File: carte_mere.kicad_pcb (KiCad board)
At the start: 4 copper layers, 78 parts, among them J1 Conn_01x02_Pin, J10 Conn_01x03_Pin, J11 Conn_01x03_Pin, J12 Conn_01x03_Pin, J13 Conn_01x03_Pin, J14 Conn_01x03_Pin, J15 Conn_01x03_Pin, J2 Conn_01x03_Pin, J25 Conn_01x02_Pin, J26 Conn_01x02_Pin, J27 Conn_01x02_Pin, J28 Conn_01x02_Pin, J29 Conn_01x02_Pin, J3 Conn_01x03_Pin, J30 Conn_01x02_Pin, J4 Conn_01x03_Pin, J5 Conn_01x03_Pin, J6 Conn_01x03_Pin, J7 Conn_01x03_Pin, J8 Conn_01x03_Pin, J9 Conn_01x03_Pin, Q1 MMBT3906, Q10 2N7002, Q11 MMBT3906, Q12 AO3401A, Q13 2N7002, Q14 MMBT3906, Q15 AO3401A, Q16 2N7002, Q17 MMBT3906, Q18 AO3401A, Q2 2N7002, Q3 AO3401A, Q4 2N7002, Q5 MMBT3906, Q6 AO3401A, Q7 2N7002, Q8 MMBT3906, Q9 AO3401A, U1 SN65HVD230, U2 SN74LVC1T45DBV, U3 R-78B3.3-2.0, U4 R-78B5.0-2.0

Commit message: update
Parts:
- removed C1, C2: 22uF, Capacitor_SMD:CP_Elec_5x5.4
- removed D3, D4: D_Small, Diode_SMD:D_SMA_Handsoldering
- removed J11, J12, J13, J14, J15: Conn_01x03_Pin, Connector_JST:JST_XH_B3B-XH-AM_1x03_P2.50mm_Vertical
- removed U3: R-78B3.3-2.0, Converter_DCDC:Converter_DCDC_RECOM_R-78B-2.0_THT
- removed U4: R-78B5.0-2.0, Converter_DCDC:Converter_DCDC_RECOM_R-78B-2.0_THT
- added C10: 47µF 6.3V, Capacitor_SMD:C_0805_2012Metric, F.Cu at (178.2, 113.8)
- added C11: 47µF 6.3V, Capacitor_SMD:C_0805_2012Metric, F.Cu at (178.2, 117.9)
- added C12: 47µF 6.3V, Capacitor_SMD:C_0805_2012Metric, F.Cu at (178.2, 120.0)
- added C13: 22µF 25V, Capacitor_SMD:C_0805_2012Metric, F.Cu at (191.0, 122.6)
- added C14: 22µF 25V, Capacitor_SMD:C_0805_2012Metric, F.Cu at (202.4, 119.5)
- added C15: 220nF 16V, Capacitor_SMD:C_0402_1005Metric, F.Cu at (202.6, 112.5)
- added C16: 150pF 50V, Capacitor_SMD:C_0603_1608Metric, F.Cu at (207.1, 116.7)
- added C17: 22µF 25V, Capacitor_SMD:C_0805_2012Metric, F.Cu at (192.1, 113.0)
- added C18: 22µF 25V, Capacitor_SMD:C_0805_2012Metric, F.Cu at (192.1, 115.2)
- added C19: 22µF 25V, Capacitor_SMD:C_0805_2012Metric, F.Cu at (192.1, 119.4)
- added C20: 22µF 25V, Capacitor_SMD:C_0805_2012Metric, F.Cu at (192.1, 117.3)
- added C21: 22µF 25V, Capacitor_SMD:C_0805_2012Metric, F.Cu at (200.9, 122.5)
- added C22: 22µF 25V, Capacitor_SMD:C_0805_2012Metric, F.Cu at (204.7, 119.5)
- added C3: 22µF 25V, Capacitor_SMD:C_0805_2012Metric, F.Cu at (180.1, 122.4)
- added C4: 22µF 25V, Capacitor_SMD:C_0805_2012Metric, F.Cu at (165.8, 114.5)
- added C5: 22µF 25V, Capacitor_SMD:C_0805_2012Metric, F.Cu at (168.0, 114.5)
- added C6: 220nF 16V, Capacitor_SMD:C_0402_1005Metric, F.Cu at (168.1, 120.5)
- added C7: 150pF 50V, Capacitor_SMD:C_0603_1608Metric, F.Cu at (163.4, 116.1)
- added C8: 47µF 6.3V, Capacitor_SMD:C_0805_2012Metric, F.Cu at (169.1, 111.5)
- added C9: 47µF 6.3V, Capacitor_SMD:C_0805_2012Metric, F.Cu at (178.2, 115.8)
- added D1: LED, LED_SMD:LED_0201_0603Metric_Pad0.64x0.40mm_HandSolder, F.Cu at (165.7, 106.3)
- added D2: LED, LED_SMD:LED_0201_0603Metric_Pad0.64x0.40mm_HandSolder, F.Cu at (180.6, 87.6)
- added J16: Conn_01x03_Pin, 7Robot_Conn:Molex_SPOX_5267-03A_1x03_P2.50mm_Vertical, F.Cu at (185.6, 83.0)
- added J17: Conn_01x05_Pin, Connector_PinHeader_2.54mm:PinHeader_1x05_P2.54mm_Vertical, F.Cu at (126.1, 104.5)
- added J18: Conn_01x05_Pin, Connector_PinHeader_2.54mm:PinHeader_1x05_P2.54mm_Vertical, F.Cu at (130.8, 104.5)
- added J19: Conn_01x05_Pin, Connector_PinHeader_2.54mm:PinHeader_1x05_P2.54mm_Vertical, F.Cu at (135.4, 104.5)
- added J31: Conn_01x03_Pin, Connector_JST:JST_XH_B3B-XH-AM_1x03_P2.50mm_Vertical, F.Cu at (92.2, 56.8)
- added J32: Conn_01x03_Pin, Connector_JST:JST_XH_B3B-XH-AM_1x03_P2.50mm_Vertical, F.Cu at (92.2, 64.6)
- added J33: Conn_01x03_Pin, Connector_JST:JST_XH_B3B-XH-AM_1x03_P2.50mm_Vertical, F.Cu at (92.2, 72.4)
- added J34: Conn_01x03_Pin, Connector_JST:JST_XH_B3B-XH-AM_1x03_P2.50mm_Vertical, F.Cu at (92.2, 80.2)
- added J35: Conn_01x03_Pin, Connector_JST:JST_XH_B3B-XH-AM_1x03_P2.50mm_Vertical, F.Cu at (104.2, 56.8)
- added J36: Conn_01x03_Pin, Connector_JST:JST_XH_B3B-XH-AM_1x03_P2.50mm_Vertical, F.Cu at (104.2, 64.6)
- added J37: Conn_01x03_Pin, Connector_JST:JST_XH_B3B-XH-AM_1x03_P2.50mm_Vertical, F.Cu at (104.2, 72.4)
- added J38: Conn_01x03_Pin, Connector_JST:JST_XH_B3B-XH-AM_1x03_P2.50mm_Vertical, F.Cu at (104.2, 80.2)
- added JP1: ~, Z7-lite:Z7-lite, F.Cu at (157.8, 55.9)
- added L1: PSPMAQ0605H-150M-ANP, 7Robot_lib:Prod_Tech_7.1x6.6mm, F.Cu at (172.8, 117.2)
- added L2: PSPMAQ0605H-150M-ANP, 7Robot_lib:Prod_Tech_7.1x6.6mm, F.Cu at (197.6, 115.8)
- added Q19: 2N7002, Package_TO_SOT_SMD:SOT-23, F.Cu at (67.3, 87.0)
- added Q20: 2N7002, Package_TO_SOT_SMD:SOT-23, F.Cu at (67.3, 91.6)
- added Q21: 2N7002, Package_TO_SOT_SMD:SOT-23, F.Cu at (67.3, 96.2)
- added Q22: 2N7002, Package_TO_SOT_SMD:SOT-23, F.Cu at (67.3, 100.9)
- added Q23: 2N7002, Package_TO_SOT_SMD:SOT-23, F.Cu at (72.2, 87.0)
- added Q24: 2N7002, Package_TO_SOT_SMD:SOT-23, F.Cu at (72.2, 91.6)
- added Q25: 2N7002, Package_TO_SOT_SMD:SOT-23, F.Cu at (72.2, 96.2)
- added Q26: 2N7002, Package_TO_SOT_SMD:SOT-23, F.Cu at (72.2, 100.9)
- added Q27: 2N7002, Package_TO_SOT_SMD:SOT-23, F.Cu at (77.1, 87.0)
- added Q28: 2N7002, Package_TO_SOT_SMD:SOT-23, F.Cu at (77.1, 91.6)
- added Q29: 2N7002, Package_TO_SOT_SMD:SOT-23, F.Cu at (77.1, 96.2)
- added Q30: 2N7002, Package_TO_SOT_SMD:SOT-23, F.Cu at (77.1, 100.9)
- added Q31: 2N7002, Package_TO_SOT_SMD:SOT-23, F.Cu at (82.0, 87.0)
- added Q32: 2N7002, Package_TO_SOT_SMD:SOT-23, F.Cu at (82.0, 91.6)
- added Q33: 2N7002, Package_TO_SOT_SMD:SOT-23, F.Cu at (82.0, 96.2)
- added Q34: 2N7002, Package_TO_SOT_SMD:SOT-23, F.Cu at (82.0, 100.9)
- added R1: 100R, Resistor_SMD:R_0201_0603Metric_Pad0.64x0.40mm_HandSolder, F.Cu at (162.2, 101.6)
- added R10: 1k, Resistor_SMD:R_0201_0603Metric_Pad0.64x0.40mm_HandSolder, F.Cu at (139.1, 106.6)
- added R100: 10k, Resistor_SMD:R_0201_0603Metric_Pad0.64x0.40mm_HandSolder, F.Cu at (99.8, 96.0)
- added R101: 10k, Resistor_SMD:R_0201_0603Metric_Pad0.64x0.40mm_HandSolder, F.Cu at (99.8, 97.7)
- added R103: 9.1k, Resistor_SMD:R_0603_1608Metric, F.Cu at (207.1, 113.5)
- added R104: 68k, Resistor_SMD:R_0603_1608Metric, F.Cu at (207.9, 120.0)
- added R11: 10k, Resistor_SMD:R_0201_0603Metric_Pad0.64x0.40mm_HandSolder, F.Cu at (85.8, 90.7)
- added R12: 2k, Resistor_SMD:R_0201_0603Metric_Pad0.64x0.40mm_HandSolder, F.Cu at (139.1, 108.3)
- added R13: 100R, Resistor_SMD:R_0201_0603Metric_Pad0.64x0.40mm_HandSolder, F.Cu at (85.8, 92.5)
- added R14: 1k, Resistor_SMD:R_0201_0603Metric_Pad0.64x0.40mm_HandSolder, F.Cu at (139.1, 110.1)
- added R15: 10k, Resistor_SMD:R_0201_0603Metric_Pad0.64x0.40mm_HandSolder, F.Cu at (85.8, 94.2)
- added R16: 2k, Resistor_SMD:R_0201_0603Metric_Pad0.64x0.40mm_HandSolder, F.Cu at (139.1, 111.8)
- added R17: 100R, Resistor_SMD:R_0201_0603Metric_Pad0.64x0.40mm_HandSolder, F.Cu at (85.8, 96.0)
- added R18: 10k, Resistor_SMD:R_0201_0603Metric_Pad0.64x0.40mm_HandSolder, F.Cu at (85.8, 97.7)
- added R19: 100R, Resistor_SMD:R_0201_0603Metric_Pad0.64x0.40mm_HandSolder, F.Cu at (88.6, 85.5)
- added R2: 100R, Resistor_SMD:R_0201_0603Metric_Pad0.64x0.40mm_HandSolder, F.Cu at (162.1, 104.5)
- added R20: 1k, Resistor_SMD:R_0201_0603Metric_Pad0.64x0.40mm_HandSolder, F.Cu at (139.1, 113.6)
- added R21: 2k, Resistor_SMD:R_0201_0603Metric_Pad0.64x0.40mm_HandSolder, F.Cu at (141.9, 103.1)
- added R22: 1k, Resistor_SMD:R_0201_0603Metric_Pad0.64x0.40mm_HandSolder, F.Cu at (141.9, 104.8)
- added R23: 10k, Resistor_SMD:R_0201_0603Metric_Pad0.64x0.40mm_HandSolder, F.Cu at (88.6, 87.2)
- added R24: 10k, Resistor_SMD:R_0201_0603Metric_Pad0.64x0.40mm_HandSolder, F.Cu at (88.6, 89.0)
- added R25: 10k, Resistor_SMD:R_0201_0603Metric_Pad0.64x0.40mm_HandSolder, F.Cu at (88.6, 90.7)
- added R26: 2k, Resistor_SMD:R_0201_0603Metric_Pad0.64x0.40mm_HandSolder, F.Cu at (141.9, 106.6)
- added R27: 1k, Resistor_SMD:R_0201_0603Metric_Pad0.64x0.40mm_HandSolder, F.Cu at (141.9, 108.3)
- added R28: 2k, Resistor_SMD:R_0201_0603Metric_Pad0.64x0.40mm_HandSolder, F.Cu at (141.9, 110.1)
- added R29: 18k, Resistor_SMD:R_0603_1608Metric, F.Cu at (163.5, 119.1)
- added R3: 1k, Resistor_SMD:R_0201_0603Metric_Pad0.64x0.40mm_HandSolder, F.Cu at (163.8, 106.3)
- added R30: 1k, Resistor_SMD:R_0201_0603Metric_Pad0.64x0.40mm_HandSolder, F.Cu at (141.9, 111.8)
- added R31: 82k, Resistor_SMD:R_0603_1608Metric, F.Cu at (163.0, 113.6)
- added R32: 2k, Resistor_SMD:R_0201_0603Metric_Pad0.64x0.40mm_HandSolder, F.Cu at (141.9, 113.6)
- added R33: 1k, Resistor_SMD:R_0201_0603Metric_Pad0.64x0.40mm_HandSolder, F.Cu at (178.4, 87.6)
- added R34: 100k, Resistor_SMD:R_0201_0603Metric_Pad0.64x0.40mm_HandSolder, F.Cu at (177.8, 83.2)
- added R35: 100R, Resistor_SMD:R_0201_0603Metric_Pad0.64x0.40mm_HandSolder, F.Cu at (176.3, 86.8)
- added R36: 100R, Resistor_SMD:R_0201_0603Metric_Pad0.64x0.40mm_HandSolder, F.Cu at (181.5, 85.9)
- added R37: 10k, Resistor_SMD:R_0201_0603Metric_Pad0.64x0.40mm_HandSolder, F.Cu at (180.5, 83.2)
- added R4: 1k, Resistor_SMD:R_0201_0603Metric_Pad0.64x0.40mm_HandSolder, F.Cu at (170.7, 103.0)
- added R5: 1k, Resistor_SMD:R_0201_0603Metric_Pad0.64x0.40mm_HandSolder, F.Cu at (139.1, 103.1)
- added R6: 10k, Resistor_SMD:R_0201_0603Metric_Pad0.64x0.40mm_HandSolder, F.Cu at (85.8, 85.5)
- added R64: 20k, Resistor_SMD:R_0201_0603Metric, F.Cu at (125.3, 99.3)
- added R66: 100R, Resistor_SMD:R_0201_0603Metric_Pad0.64x0.40mm_HandSolder, F.Cu at (88.6, 92.5)
- added R67: 10k, Resistor_SMD:R_0201_0603Metric_Pad0.64x0.40mm_HandSolder, F.Cu at (88.6, 94.2)
- added R68: 10k, Resistor_SMD:R_0201_0603Metric_Pad0.64x0.40mm_HandSolder, F.Cu at (88.6, 96.0)
- added R69: 100R, Resistor_SMD:R_0201_0603Metric_Pad0.64x0.40mm_HandSolder, F.Cu at (88.6, 97.7)
- added R7: 100R, Resistor_SMD:R_0201_0603Metric_Pad0.64x0.40mm_HandSolder, F.Cu at (85.8, 87.2)
- added R70: 10k, Resistor_SMD:R_0201_0603Metric_Pad0.64x0.40mm_HandSolder, F.Cu at (91.4, 85.5)
- added R71: 10k, Resistor_SMD:R_0201_0603Metric_Pad0.64x0.40mm_HandSolder, F.Cu at (91.4, 87.2)
- added R72: 100R, Resistor_SMD:R_0201_0603Metric_Pad0.64x0.40mm_HandSolder, F.Cu at (91.4, 89.0)
- added R73: 10k, Resistor_SMD:R_0201_0603Metric_Pad0.64x0.40mm_HandSolder, F.Cu at (91.4, 90.7)
- added R74: 10k, Resistor_SMD:R_0201_0603Metric_Pad0.64x0.40mm_HandSolder, F.Cu at (91.4, 92.5)
- added R75: 100R, Resistor_SMD:R_0201_0603Metric_Pad0.64x0.40mm_HandSolder, F.Cu at (91.4, 94.2)
- added R76: 10k, Resistor_SMD:R_0201_0603Metric_Pad0.64x0.40mm_HandSolder, F.Cu at (91.4, 96.0)
- added R77: 10k, Resistor_SMD:R_0201_0603Metric_Pad0.64x0.40mm_HandSolder, F.Cu at (91.4, 97.7)
- added R78: 100R, Resistor_SMD:R_0201_0603Metric_Pad0.64x0.40mm_HandSolder, F.Cu at (94.2, 85.5)
- added R79: 10k, Resistor_SMD:R_0201_0603Metric_Pad0.64x0.40mm_HandSolder, F.Cu at (94.2, 87.2)
- added R8: 2k, Resistor_SMD:R_0201_0603Metric_Pad0.64x0.40mm_HandSolder, F.Cu at (139.1, 104.8)
- added R80: 10k, Resistor_SMD:R_0201_0603Metric_Pad0.64x0.40mm_HandSolder, F.Cu at (94.2, 89.0)
- added R81: 100R, Resistor_SMD:R_0201_0603Metric_Pad0.64x0.40mm_HandSolder, F.Cu at (94.2, 90.7)
- added R82: 10k, Resistor_SMD:R_0201_0603Metric_Pad0.64x0.40mm_HandSolder, F.Cu at (94.2, 92.5)
- added R83: 10k, Resistor_SMD:R_0201_0603Metric_Pad0.64x0.40mm_HandSolder, F.Cu at (94.2, 94.2)
- added R84: 100R, Resistor_SMD:R_0201_0603Metric_Pad0.64x0.40mm_HandSolder, F.Cu at (94.2, 96.0)
- added R85: 10k, Resistor_SMD:R_0201_0603Metric_Pad0.64x0.40mm_HandSolder, F.Cu at (94.2, 97.7)
- added R86: 10k, Resistor_SMD:R_0201_0603Metric_Pad0.64x0.40mm_HandSolder, F.Cu at (97.0, 85.5)
- added R87: 100R, Resistor_SMD:R_0201_0603Metric_Pad0.64x0.40mm_HandSolder, F.Cu at (97.0, 87.2)
- added R88: 10k, Resistor_SMD:R_0201_0603Metric_Pad0.64x0.40mm_HandSolder, F.Cu at (97.0, 89.0)
- added R89: 10k, Resistor_SMD:R_0201_0603Metric_Pad0.64x0.40mm_HandSolder, F.Cu at (97.0, 90.7)
- added R9: 10k, Resistor_SMD:R_0201_0603Metric_Pad0.64x0.40mm_HandSolder, F.Cu at (85.8, 89.0)
- added R90: 100R, Resistor_SMD:R_0201_0603Metric_Pad0.64x0.40mm_HandSolder, F.Cu at (97.0, 92.5)
- added R91: 10k, Resistor_SMD:R_0201_0603Metric_Pad0.64x0.40mm_HandSolder, F.Cu at (97.0, 94.2)
- added R92: 10k, Resistor_SMD:R_0201_0603Metric_Pad0.64x0.40mm_HandSolder, F.Cu at (97.0, 96.0)
- added R93: 100R, Resistor_SMD:R_0201_0603Metric_Pad0.64x0.40mm_HandSolder, F.Cu at (97.0, 97.7)
- added R94: 10k, Resistor_SMD:R_0201_0603Metric_Pad0.64x0.40mm_HandSolder, F.Cu at (99.8, 85.5)
- added R95: 10k, Resistor_SMD:R_0201_0603Metric_Pad0.64x0.40mm_HandSolder, F.Cu at (99.8, 87.2)
- added R96: 100R, Resistor_SMD:R_0201_0603Metric_Pad0.64x0.40mm_HandSolder, F.Cu at (99.8, 89.0)
- added R97: 10k, Resistor_SMD:R_0201_0603Metric_Pad0.64x0.40mm_HandSolder, F.Cu at (99.8, 90.7)
- added R98: 10k, Resistor_SMD:R_0201_0603Metric_Pad0.64x0.40mm_HandSolder, F.Cu at (99.8, 92.5)
- added R99: 100R, Resistor_SMD:R_0201_0603Metric_Pad0.64x0.40mm_HandSolder, F.Cu at (99.8, 94.2)
- added U5: TPS54302, Package_TO_SOT_SMD:SOT-23-6, F.Cu at (166.9, 118.1)
- added U6: TPS54302, Package_TO_SOT_SMD:SOT-23-6, F.Cu at (203.5, 114.9)
- J10: value Conn_01x03_Pin -> Conn_01x02_Pin; footprint Connector_JST:JST_XH_B3B-XH-AM_1x03_P2.50mm_Vertical -> Connector_AMASS:AMASS_XT30U-F_1x02_P5.0mm_Vertical
- moved J1 270.8 mm to (173.9, 104.3), turned to 90 degrees
- moved H3 265.7 mm to (209.3, 125.0)
- moved U1 261.3 mm to (166.4, 103.0)
- moved U2 258.3 mm to (178.9, 85.4)
- moved J10 237.9 mm to (185.9, 115.0), turned to -90 degrees
- moved R38 233.2 mm to (144.8, 103.1)
- moved R39 233.2 mm to (144.8, 104.8)
- moved R40 233.2 mm to (144.8, 106.6)
- moved R41 233.2 mm to (144.8, 108.3)
- moved J25 216.3 mm to (118.1, 56.8)
- moved J27 216.3 mm to (118.1, 72.4)
- moved J28 216.3 mm to (118.1, 80.2)
- moved J29 216.3 mm to (118.1, 88.0)
- moved J30 216.3 mm to (118.1, 95.8)
- moved Q13 216.3 mm to (136.3, 62.5)
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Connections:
- net +5V renamed 5V
- J10 pad 2: 5V_POWER -> 24V
- U1 pad 3: +3V3 -> 3.3V
- U2 pad 1: +3.3V -> 3.3V
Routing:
- net GND: track 0.00 -> 25.1 mm, vias 0 -> 56
- net 3.3V: track 0.00 -> 19.8 mm, vias 0 -> 19
- net 5V: track 0.00 -> 15.5 mm, vias 0 -> 15
- net Net-(U6-SW): track 0.00 -> 11.0 mm
- net Net-(U5-SW): track 0.00 -> 9.71 mm
- net Net-(U6-FB): track 0.00 -> 8.79 mm
- net Net-(U5-FB): track 0.00 -> 7.74 mm
- net Net-(J16-Pin_1): track 0.00 -> 6.86 mm
- net /CAN/CAN_L: track 0.00 -> 5.50 mm
- net /CAN/CAN_H: track 0.00 -> 5.44 mm
- net AX_DIR: track 0.00 -> 3.61 mm
- net Net-(U1-R): track 0.00 -> 3.41 mm
- net CAND: track 0.00 -> 2.69 mm
- net Net-(U5-BOOT): track 0.00 -> 2.44 mm
- net Net-(U6-BOOT): track 0.00 -> 2.14 mm
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- added copper zone on F.Cu, net 24V
- added copper zone on F.Cu, net 3.3V
- added copper zone on F.Cu, net 5V
- added copper zone on F.Cu, net GND
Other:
- board outline added: 80 x 80 mm

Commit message: update schematic + layout
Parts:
- removed J17, J18, J19: Conn_01x05_Pin, Connector_PinHeader_2.54mm:PinHeader_1x05_P2.54mm_Vertical
- removed R10, R14, R20, R22, R27, R30, R38, R40, R5: 1k, Resistor_SMD:R_0201_0603Metric_Pad0.64x0.40mm_HandSolder
- removed R12, R16, R21, R26, R28, R32, R39, R41, R8: 2k, Resistor_SMD:R_0201_0603Metric_Pad0.64x0.40mm_HandSolder
- R45, R49, R53, R57, R61, R65: footprint Resistor_SMD:R_1020_2550Metric_Pad1.33x5.20mm_HandSolder -> Resistor_SMD:R_2010_5025Metric
- moved Q25 128.5 mm to (193.8, 54.7), turned to 90 degrees
- moved Q26 127.6 mm to (193.6, 61.9), turned to 90 degrees
- moved Q19 125.6 mm to (188.3, 53.5), turned to 90 degrees
- moved Q20 125.0 mm to (188.4, 60.6), turned to 90 degrees
- moved Q21 124.3 mm to (188.3, 67.8), turned to 90 degrees
- moved Q22 123.7 mm to (188.3, 75.2), turned to 90 degrees
- moved H1 121.6 mm to (228.0, 53.5)
- moved J8 120.8 mm to (198.4, 97.3)
- moved J9 120.6 mm to (198.4, 104.7)
- moved Q27 117.9 mm to (193.6, 69.3), turned to 90 degrees
- moved Q28 117.5 mm to (193.6, 76.7), turned to 90 degrees
- moved Q29 117.2 mm to (193.6, 83.8), turned to 90 degrees
- moved Q30 116.9 mm to (193.6, 91.1), turned to 90 degrees
- moved Q24 116.9 mm to (188.3, 104.9), turned to 90 degrees
- moved Q23 116.6 mm to (188.3, 97.6), turned to 90 degrees
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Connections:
- JP1 pad JP1_1: CANR -> CAND
- JP1 pad JP1_2: unconnected-(JP1-P18-PadJP1_2) -> CANR
- JP1 pad JP1_3: CAND -> unconnected-(JP1-R16-PadJP1_3)
- JP1 pad JP2_24: DSO_3 -> DSO_6
- JP1 pad JP2_26: DSO_4 -> DSO_3
- JP1 pad JP2_28: DSO_5 -> DSO_4
- JP1 pad JP2_32: DSO_6 -> DSO_5
- R50 pad 2: DSO_2 -> DSO_6
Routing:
- net 5V_POWER: track 0.00 -> 112.7 mm
- net GND: track 25.1 -> 134.5 mm, vias 56 -> 81
- net SERVO8: track 0.00 -> 62.7 mm, vias 0 -> 2
- net SERVO7: track 0.00 -> 54.9 mm, vias 0 -> 2
- net SERVO6: track 0.00 -> 51.5 mm, vias 0 -> 2
- net SERVO5: track 0.00 -> 41.7 mm, vias 0 -> 2
- net SERVO4: track 0.00 -> 38.3 mm, vias 0 -> 2
- net 12V: track 0.00 -> 31.1 mm, vias 0 -> 16
- net SERVO15: track 0.00 -> 30.2 mm
- net SERVO3: track 0.00 -> 29.7 mm
- net SERVO2: track 0.00 -> 28.7 mm
- net SERVO14: track 0.00 -> 25.3 mm
- net SERVO9: track 0.00 -> 24.6 mm, vias 0 -> 1
- net SERVO13: track 0.00 -> 23.3 mm
- net SERVO10: track 0.00 -> 22.7 mm, vias 0 -> 1
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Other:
- board size 80 x 80 mm -> 82 x 85 mm

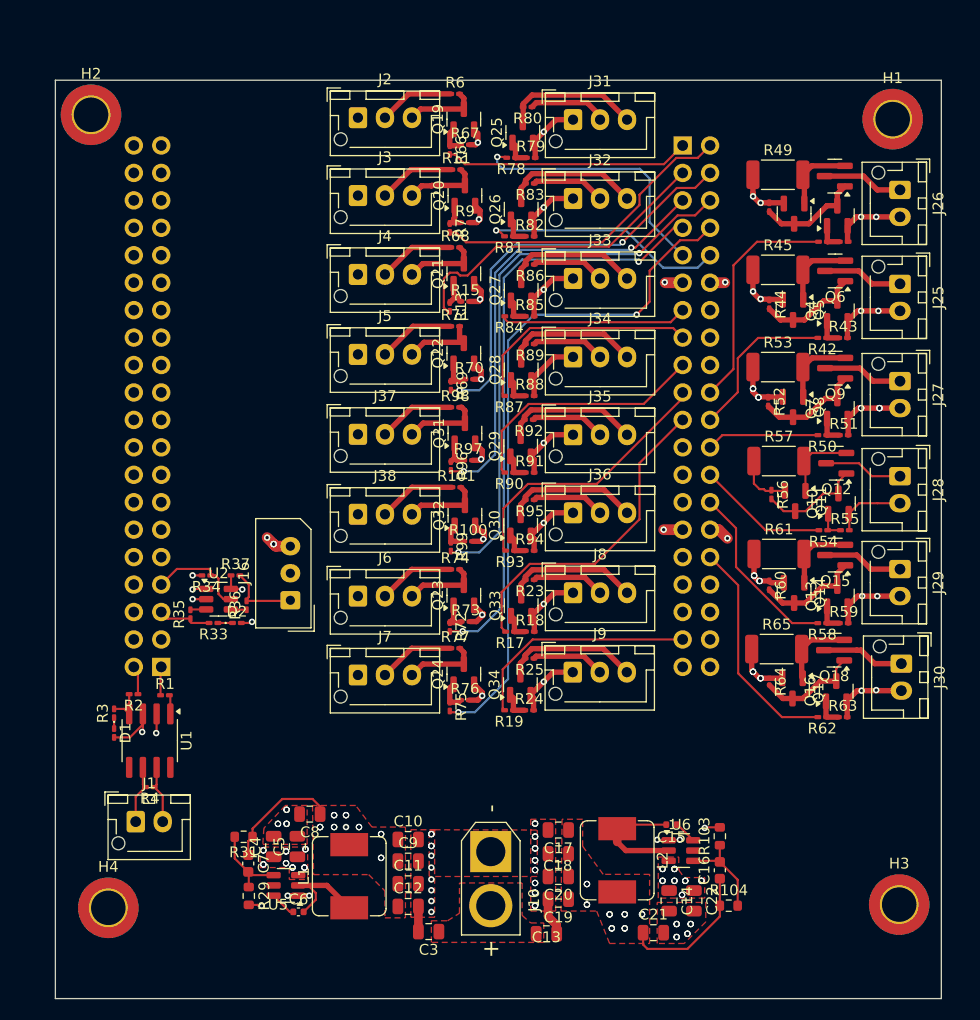
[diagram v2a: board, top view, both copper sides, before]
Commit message: v1 - need to change resistor package
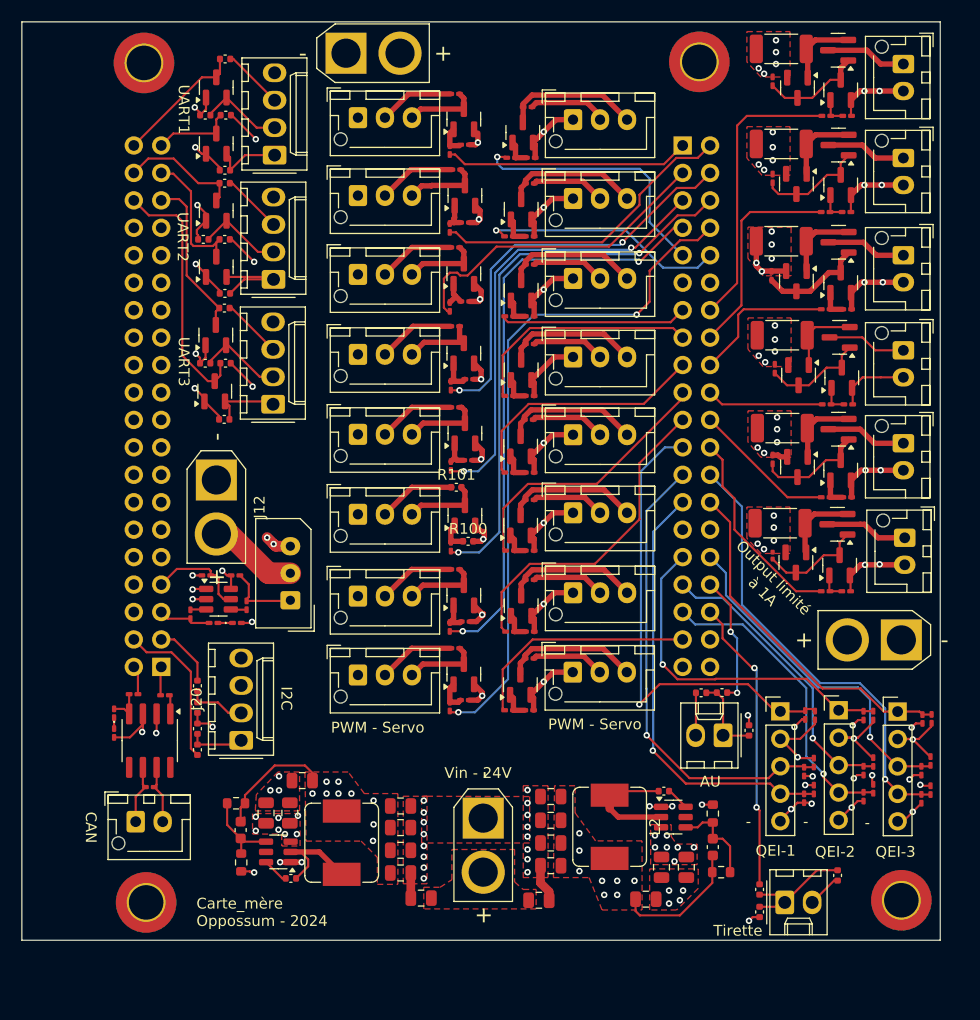
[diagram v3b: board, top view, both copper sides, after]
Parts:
- removed H4: MountingHole_Pad_MP, MountingHole:MountingHole_3.2mm_M3_DIN965_Pad_TopBottom
- added H5: MountingHole_Pad, MountingHole:MountingHole_3.2mm_M3_DIN965_Pad_TopBottom, F.Cu at (158.9, 126.0)
- added J11: Conn_01x02_Pin, Connector_AMASS:AMASS_XT30U-F_1x02_P5.0mm_Vertical, F.Cu at (177.4, 47.4)
- added J12: Conn_01x02_Pin, Connector_AMASS:AMASS_XT30U-F_1x02_P5.0mm_Vertical, F.Cu at (165.4, 86.9)
- added J13: Conn_01x02_Pin, Connector_AMASS:AMASS_XT30U-F_1x02_P5.0mm_Vertical, F.Cu at (228.8, 101.7)
- added J14: Conn_01x02, Connector_Molex:Molex_KK-254_AE-6410-02A_1x02_P2.54mm_Vertical, F.Cu at (218.0, 126.0)
- added J15: Conn_01x04, Connector_Molex:Molex_KK-254_AE-6410-04A_1x04_P2.54mm_Vertical, F.Cu at (170.7, 79.9)
- added J17: Conn_01x05_Pin, Connector_PinHeader_2.54mm:PinHeader_1x05_P2.54mm_Vertical, F.Cu at (217.6, 108.3)
- added J18: Conn_01x05_Pin, Connector_PinHeader_2.54mm:PinHeader_1x05_P2.54mm_Vertical, F.Cu at (223.0, 108.2)
- added J19: Conn_01x05_Pin, Connector_PinHeader_2.54mm:PinHeader_1x05_P2.54mm_Vertical, F.Cu at (228.5, 108.3)
- added J20: Conn_01x04, Connector_Molex:Molex_KK-254_AE-6410-04A_1x04_P2.54mm_Vertical, F.Cu at (167.7, 111.0)
- added J21: Conn_01x04, Connector_Molex:Molex_KK-254_AE-6410-04A_1x04_P2.54mm_Vertical, F.Cu at (170.7, 68.3)
- added J22: Conn_01x04, Connector_Molex:Molex_KK-254_AE-6410-04A_1x04_P2.54mm_Vertical, F.Cu at (170.8, 56.8)
- added J23: Conn_01x02, Connector_Molex:Molex_KK-254_AE-6410-02A_1x02_P2.54mm_Vertical, F.Cu at (212.3, 110.5)
- added Q35: 2N7002, Package_TO_SOT_SMD:SOT-23, F.Cu at (165.2, 78.7)
- added Q36: 2N7002, Package_TO_SOT_SMD:SOT-23, F.Cu at (165.3, 73.5)
- added Q37: 2N7002, Package_TO_SOT_SMD:SOT-23, F.Cu at (165.4, 67.2)
- added Q38: 2N7002, Package_TO_SOT_SMD:SOT-23, F.Cu at (165.4, 62.0)
- added Q39: 2N7002, Package_TO_SOT_SMD:SOT-23, F.Cu at (165.4, 55.8)
- added Q40: 2N7002, Package_TO_SOT_SMD:SOT-23, F.Cu at (165.4, 50.6)
- added R10: 1k, Resistor_SMD:R_0201_0603Metric_Pad0.64x0.40mm_HandSolder, F.Cu at (226.2, 115.5)
- added R102: 10k, Capacitor_SMD:C_0402_1005Metric, F.Cu at (166.1, 81.3)
- added R105: 10k, Capacitor_SMD:C_0402_1005Metric, F.Cu at (164.4, 76.1)
- added R106: 10k, Capacitor_SMD:C_0402_1005Metric, F.Cu at (166.2, 76.1)
- added R107: 10k, Capacitor_SMD:C_0402_1005Metric, F.Cu at (166.2, 71.0)
- added R108: 10k, Capacitor_SMD:C_0402_1005Metric, F.Cu at (166.2, 69.6)
- added R109: 10k, Capacitor_SMD:C_0402_1005Metric, F.Cu at (164.2, 64.6)
- added R110: 10k, Capacitor_SMD:C_0402_1005Metric, F.Cu at (166.2, 64.6)
- added R111: 10k, Capacitor_SMD:C_0402_1005Metric, F.Cu at (166.2, 59.4)
- added R112: 10k, Capacitor_SMD:C_0402_1005Metric, F.Cu at (166.2, 58.2)
- added R113: 10k, Capacitor_SMD:C_0402_1005Metric, F.Cu at (164.4, 53.1)
- added R114: 10k, Capacitor_SMD:C_0402_1005Metric, F.Cu at (166.3, 53.1)
- added R115: 10k, Capacitor_SMD:C_0402_1005Metric, F.Cu at (166.2, 47.9)
- added R116: 1k, Capacitor_SMD:C_0402_1005Metric, F.Cu at (215.7, 126.9)
- added R117: 2k, Capacitor_SMD:C_0402_1005Metric, F.Cu at (222.9, 123.5)
- added R118: 100k, Capacitor_SMD:C_0402_1005Metric, F.Cu at (163.7, 109.9)
- added R119: 100k, Capacitor_SMD:C_0402_1005Metric, F.Cu at (163.7, 108.0)
- added R12: 2k, Resistor_SMD:R_0201_0603Metric_Pad0.64x0.40mm_HandSolder, F.Cu at (225.3, 116.2)
- added R120: 100R, Capacitor_SMD:C_0402_1005Metric, F.Cu at (215.7, 124.8)
- added R121: 100R, Capacitor_SMD:C_0402_1005Metric, F.Cu at (163.7, 111.9)
- added R122: 100R, Capacitor_SMD:C_0402_1005Metric, F.Cu at (163.7, 106.0)
- added R123: 100R, Capacitor_SMD:C_0402_1005Metric, F.Cu at (212.2, 106.6)
- added R124: 1k, Capacitor_SMD:C_0402_1005Metric, F.Cu at (214.7, 110.1)
- added R125: 2k, Capacitor_SMD:C_0402_1005Metric, F.Cu at (210.3, 106.6)
- added R14: 1k, Resistor_SMD:R_0201_0603Metric_Pad0.64x0.40mm_HandSolder, F.Cu at (231.5, 115.6)
- added R16: 2k, Resistor_SMD:R_0201_0603Metric_Pad0.64x0.40mm_HandSolder, F.Cu at (230.7, 116.4)
- added R20: 1k, Resistor_SMD:R_0201_0603Metric_Pad0.64x0.40mm_HandSolder, F.Cu at (220.7, 113.1)
- added R21: 2k, Resistor_SMD:R_0201_0603Metric_Pad0.64x0.40mm_HandSolder, F.Cu at (219.8, 113.9)
- added R22: 1k, Resistor_SMD:R_0201_0603Metric_Pad0.64x0.40mm_HandSolder, F.Cu at (226.2, 113.0)
- added R26: 2k, Resistor_SMD:R_0201_0603Metric_Pad0.64x0.40mm_HandSolder, F.Cu at (225.3, 113.8)
- added R27: 1k, Resistor_SMD:R_0201_0603Metric_Pad0.64x0.40mm_HandSolder, F.Cu at (231.5, 112.9)
- added R28: 2k, Resistor_SMD:R_0201_0603Metric_Pad0.64x0.40mm_HandSolder, F.Cu at (230.7, 113.8)
- added R30: 1k, Resistor_SMD:R_0201_0603Metric_Pad0.64x0.40mm_HandSolder, F.Cu at (220.8, 108.7)
- added R32: 2k, Resistor_SMD:R_0201_0603Metric_Pad0.64x0.40mm_HandSolder, F.Cu at (219.9, 108.7)
- added R38: 1k, Resistor_SMD:R_0201_0603Metric_Pad0.64x0.40mm_HandSolder, F.Cu at (226.2, 108.7)
- added R39: 2k, Resistor_SMD:R_0201_0603Metric_Pad0.64x0.40mm_HandSolder, F.Cu at (225.3, 108.7)
- added R40: 1k, Resistor_SMD:R_0201_0603Metric_Pad0.64x0.40mm_HandSolder, F.Cu at (231.6, 109.0)
- added R41: 2k, Resistor_SMD:R_0201_0603Metric_Pad0.64x0.40mm_HandSolder, F.Cu at (230.8, 109.0)
- added R5: 1k, Resistor_SMD:R_0201_0603Metric_Pad0.64x0.40mm_HandSolder, F.Cu at (220.7, 115.6)
- added R8: 2k, Resistor_SMD:R_0201_0603Metric_Pad0.64x0.40mm_HandSolder, F.Cu at (219.8, 116.4)
- H1, H2, H3: value MountingHole_Pad_MP -> MountingHole_Pad
- R100, R101: footprint Resistor_SMD:R_0201_0603Metric_Pad0.64x0.40mm_HandSolder -> Capacitor_SMD:C_0402_1005Metric
- moved H1 18.7 mm to (210.1, 48.2)
- moved J27 11.7 mm to (229.0, 66.1)
- moved J29 11.7 mm to (229.0, 83.5)
- moved J30 11.7 mm to (229.1, 92.2)
- moved Q10 11.7 mm to (223.3, 77.4)
- moved Q13 11.7 mm to (223.2, 86.0)
- moved Q16 11.7 mm to (223.1, 94.8)
- moved Q17 11.7 mm to (219.0, 94.5)
- moved Q18 11.7 mm to (222.9, 91.0)
- moved Q2 11.7 mm to (223.2, 50.8)
- moved Q5 11.7 mm to (219.1, 59.5)
- moved Q8 11.7 mm to (219.1, 68.5)
- moved R45 11.7 mm to (217.7, 55.8)
- moved R50 11.7 mm to (221.8, 71.1)
- moved R51 11.7 mm to (223.8, 71.1)
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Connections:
- H1 pad 1: (no net) -> GND
- H2 pad 1: (no net) -> GND
- H3 pad 1: (no net) -> GND
- JP1 pad JP1_3: unconnected-(JP1-R16-PadJP1_3) -> SDA
- JP1 pad JP1_35: unconnected-(JP1-U14-PadJP1_35) -> TX-lidar_1
- JP1 pad JP1_36: unconnected-(JP1-U15-PadJP1_36) -> RX-lidar_1
- JP1 pad JP1_37: unconnected-(JP1-U13-PadJP1_37) -> RX-lidar_3
- JP1 pad JP1_38: unconnected-(JP1-V13-PadJP1_38) -> TX-lidar_3
- JP1 pad JP1_39: unconnected-(JP1-T12-PadJP1_39) -> RX-lidar_2
- JP1 pad JP1_4: unconnected-(JP1-R17-PadJP1_4) -> SCL
- JP1 pad JP1_40: unconnected-(JP1-U12-PadJP1_40) -> TX-lidar_2
- JP1 pad JP2_14: QEI_3_X -> DSO_1
- JP1 pad JP2_16: QEI_3_B -> DSO_2
- JP1 pad JP2_18: QEI_3_A -> DSO_6
- JP1 pad JP2_20: DSO_1 -> DSO_3
- JP1 pad JP2_22: DSO_2 -> DSO_4
- JP1 pad JP2_24: DSO_6 -> DSO_5
- JP1 pad JP2_26: DSO_3 -> QEI_3_X
- JP1 pad JP2_28: DSO_4 -> QEI_3_A
- JP1 pad JP2_32: DSO_5 -> QEI_3_B
- JP1 pad JP2_34: unconnected-(JP1-F20-PadJP2_34) -> AU
- JP1 pad JP2_36: unconnected-(JP1-M20-PadJP2_36) -> Tirette
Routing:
- net 3.3V: track 21.5 -> 87.7 mm, vias 20 -> 18
- net 5V: track 17.1 -> 78.7 mm, vias 16 -> 21
- net QEI_1_A: track 0.00 -> 44.7 mm, vias 0 -> 1
- net QEI_1_B: track 0.00 -> 43.0 mm, vias 0 -> 1
- net QEI_3_X: track 0.00 -> 41.9 mm, vias 0 -> 1
- net QEI_1_X: track 0.00 -> 40.6 mm, vias 0 -> 1
- net QEI_3_A: track 0.00 -> 32.6 mm
- net QEI_2_A: track 0.00 -> 32.0 mm, vias 0 -> 1
- net QEI_3_B: track 0.00 -> 31.8 mm, vias 0 -> 1
- net QEI_2_X: track 0.00 -> 28.4 mm, vias 0 -> 1
- net QEI_2_B: track 0.00 -> 27.3 mm, vias 0 -> 1
- net Tirette: track 0.00 -> 27.2 mm, vias 0 -> 2
- net 12V: track 31.1 -> 6.91 mm, vias 16 -> 30
- net RX-lidar_1: track 0.00 -> 23.6 mm
- net GND: track 134.5 -> 154.8 mm, vias 81 -> 69
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- added copper zone on F.Cu, net 12V
- added copper zone on In2.Cu, net 12V
- added copper zone on In2.Cu, net 24V
- added copper zone on In2.Cu, net 3.3V
- added copper zone on In2.Cu, net 5V
- added copper zone on In2.Cu, net 5V_POWER
- added copper zone on In1.Cu, net GND
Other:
- board size 82 x 85 mm -> 85 x 85 mm
- board text added: "-"
- board text added: "AU"
- board text added: "CAN"
- board text added: "Carte_mère Oppossum - 2024"
- board text added: "I2C"
- board text added: "Output limité à 1A"
- board text added: "PWM - Servo"
- board text added: "QEI-1"
- board text added: "QEI-2"
- board text added: "QEI-3"
- board text added: "Tirette"
- board text added: "UART1"
- board text added: "UART2"
- board text added: "UART3"
- board text added: "Vin - 24V"

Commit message: add media
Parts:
- D1, D2: footprint LED_SMD:LED_0201_0603Metric_Pad0.64x0.40mm_HandSolder -> LED_SMD:LED_0402_1005Metric
- R1, R10, R11, R12, R13, R14, R15, R16, R17, R18, R19, R2, R20, R21, R22, R23, R24, R25, R26, R27, R28, R3, R30, R32, R33, R34, R35, R36, R37, R38, R39, R4, R40, R41, R42, R43, R44, R46, R47, R48, R5, R50, R51, R52, R54, R55, R56, R58, R59, R6, R60, R62, R63, R66, R67, R68, R69, R7, R70, R71, R72, R73, R74, R75, R76, R77, R78, R79, R8, R80, R81, R82, R83, R84, R85, R86, R87, R88, R89, R9, R90, R91, R92, R93, R94, R95, R96, R97, R98, R99: footprint Resistor_SMD:R_0201_0603Metric_Pad0.64x0.40mm_HandSolder -> Resistor_SMD:R_0402_1005Metric
- R64: footprint Resistor_SMD:R_0201_0603Metric -> Capacitor_SMD:C_0402_1005Metric
- moved J17 1.95 mm to (215.7, 108.3)
- moved R32 1.85 mm to (218.1, 108.8)
- moved R8 1.75 mm to (218.1, 116.3)
- moved R21 1.75 mm to (218.1, 113.9)
- moved R30 1.65 mm to (219.2, 108.8)
- moved R5 1.55 mm to (219.2, 115.5)
- moved R20 1.55 mm to (219.2, 113.0)
- moved R124 1.45 mm to (213.2, 110.2)
- moved J18 1.40 mm to (221.6, 108.2)
- moved J23 1.38 mm to (210.9, 110.6)
- moved R12 1.33 mm to (224.0, 116.5)
- moved R39 1.30 mm to (224.0, 108.6)
- moved R26 1.25 mm to (224.1, 113.8)
- moved R125 1.17 mm to (209.1, 106.6)
- moved R38 1.10 mm to (225.1, 108.7)
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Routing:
- net 5V: track 78.7 -> 70.4 mm
- net 3.3V: track 87.7 -> 92.1 mm
- net GND: track 154.8 -> 158.2 mm, vias 69 -> 68
- net QEI_1_X: track 40.6 -> 38.9 mm
- net QEI_1_A: track 44.7 -> 43.1 mm
- net DSO_5: track 18.9 -> 20.4 mm
- net 12V: track 6.91 -> 5.50 mm
- net SERVO12: track 21.9 -> 23.3 mm
- net Net-(J31-Pin_3): track 12.6 -> 13.9 mm
- net SERVO8: track 62.7 -> 63.9 mm
- net SERVO16: track 21.7 -> 22.8 mm
- net SERVO14: track 25.3 -> 26.5 mm
- net V_AX: track 8.35 -> 9.44 mm
- net SERVO7: track 54.9 -> 56.0 mm
- net Net-(Q19-G): track 2.70 -> 3.77 mm
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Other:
- board text added: "OUT-1"
- board text added: "OUT-2"
- board text added: "OUT-3"
- board text added: "OUT-4"
- board text added: "OUT-5"
- board text added: "OUT-6"
- board text added: "PWM - Servo 1 to 8"
- board text added: "PWM - Servo 9 to 16"
- board text added: "PWM-1"
- board text added: "PWM-10"
- board text added: "PWM-11"
- board text added: "PWM-12"
- board text added: "PWM-13"
- board text added: "PWM-14"
- board text added: "PWM-15"
- board text added: "PWM-16"
- board text added: "PWM-2"
- board text added: "PWM-3"
- board text added: "PWM-4"
- board text added: "PWM-5"
- board text added: "PWM-6"
- board text added: "PWM-7"
- board text added: "PWM-8"
- board text added: "PWM-9"
- board text added: "Vin - 12V"
- board text removed: "PWM - Servo"
